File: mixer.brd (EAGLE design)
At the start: 23 x 40 mm, 21 parts, among them U2 SA602AD8-SOIC

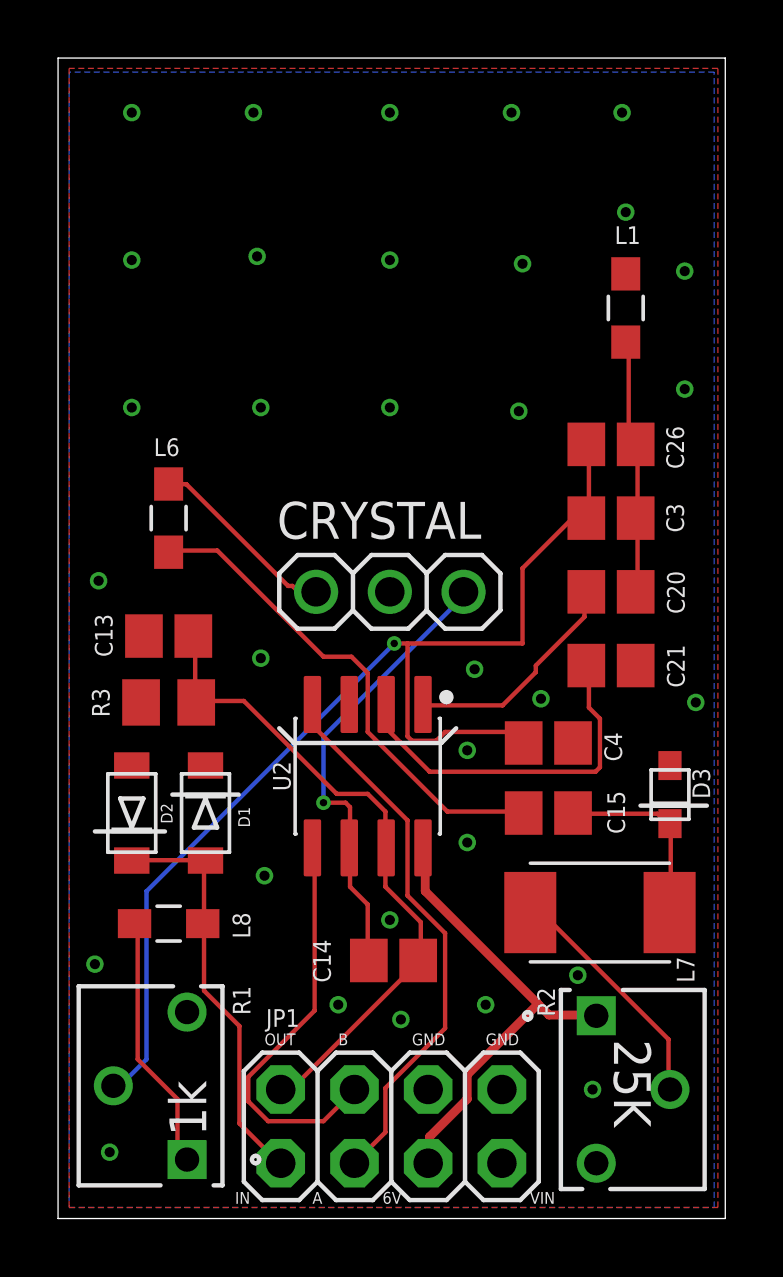
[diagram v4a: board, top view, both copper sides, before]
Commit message: Version 1.2 as ordered
* some slight cleanup in labels and routing after looking at the previews on oshpark
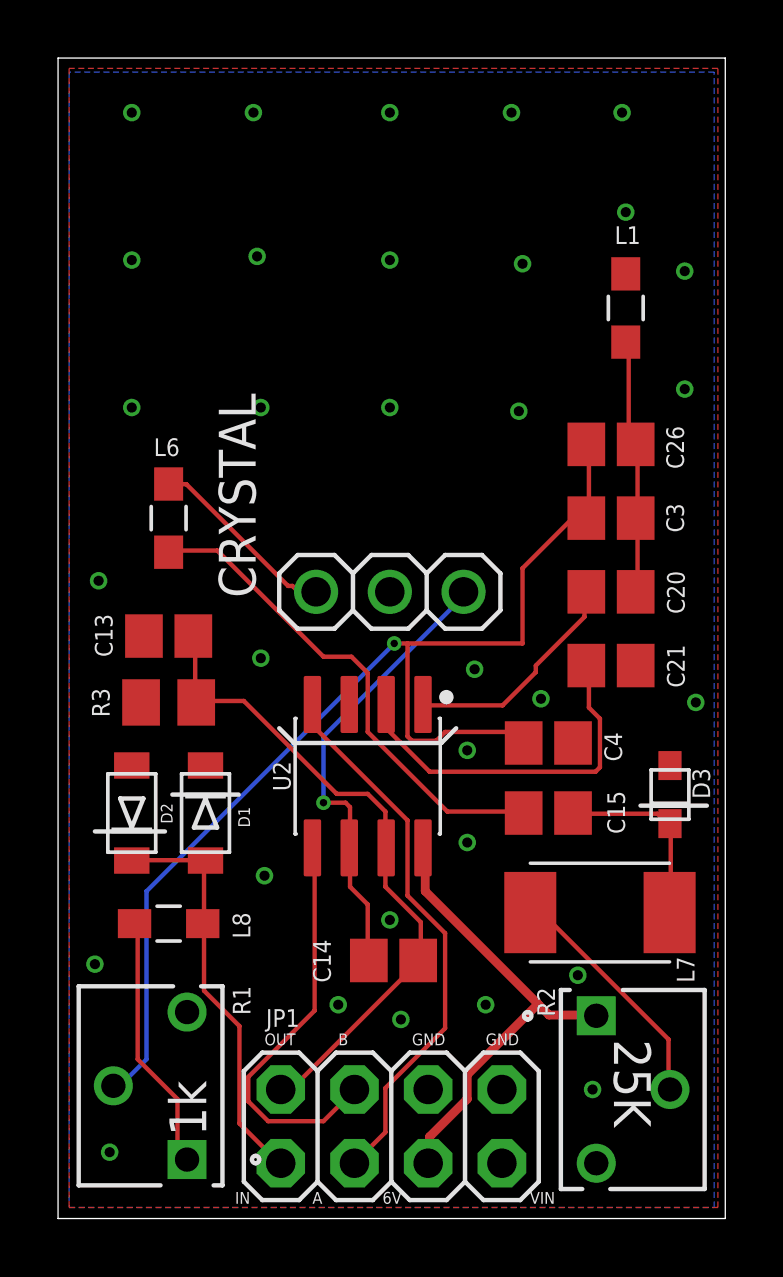
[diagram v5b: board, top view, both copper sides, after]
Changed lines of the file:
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@@
 </element>
 <element name="CRYSTAL" library="adafruit" library_urn="urn:adsk.eagle:library:420" package="1X03" package3d_urn="urn:adsk.eagle:package:6240710/1" value="" x="11.43" y="21.59" smashed="yes">
-<attribute name="NAME" x="7.5438" y="23.4188" size="1.27" layer="25" ratio="10"/>
+<attribute name="NAME" x="6.8072" y="21.3868" size="1.27" layer="25" ratio="10" rot="R90"/>
 <attribute name="VALUE" x="7.62" y="18.415" size="1.27" layer="27"/>
 </element>

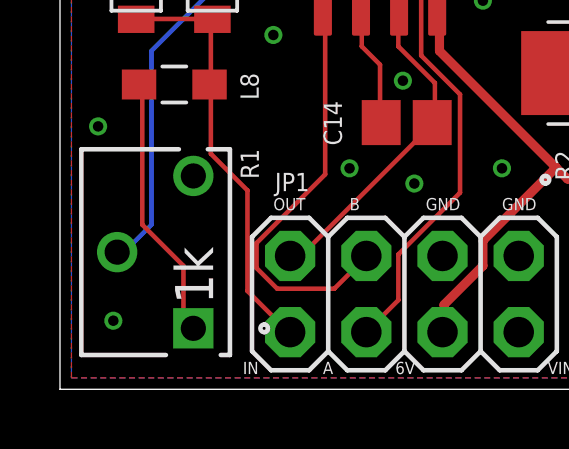
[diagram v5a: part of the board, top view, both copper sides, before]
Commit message: v1.3
* replaced L5 and C19 with larger devices capable of more current
* replaced Q2 with another 2222A
* increased power and output wire size to 15mil (from 12)

Revisions based on testing with my amplifier circuit breakout
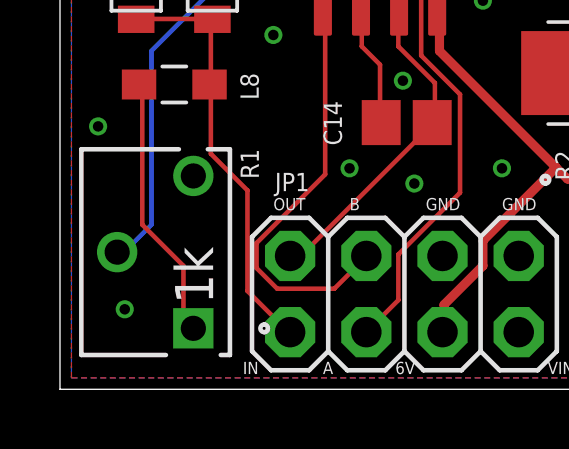
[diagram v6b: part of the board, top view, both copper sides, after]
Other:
- board text added: "9VμTX Mixer Board v1.3 K6GG & K6JCA"
- board text removed: "9VμTX Mixer Board v1.2 K6GG & K6JCA"
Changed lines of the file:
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@@
 <wire x1="0" y1="39.9796" x2="0" y2="0" width="0" layer="20"/>
 <text x="17.78" y="34.29" size="0.8128" layer="26" rot="MR0">9VμTX
-Mixer Board v1.2
+Mixer Board v1.3
 K6GG &amp; K6JCA</text>
 <text x="6.096" y="0.508" size="0.4064" layer="25">IN</text>
@@
 <via x="1.397" y="21.971" extent="1-16" drill="0.35"/>
 <via x="1.27" y="8.763" extent="1-16" drill="0.35"/>
-<via x="1.778" y="2.286" extent="1-16" drill="0.35"/>
+<via x="2.159" y="2.667" extent="1-16" drill="0.35"/>
 <contactref element="JP1" pad="6"/>
 <via x="18.415" y="4.445" extent="1-16" drill="0.35"/>
